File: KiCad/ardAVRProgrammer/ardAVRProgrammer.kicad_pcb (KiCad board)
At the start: 2 copper layers, 86.4 x 58.4 mm, 13 parts, among them J1 2x5_ISP_header, J2 2x3_ISP_header, U1 ATmega328-PU, U2 ATtiny2313-20PU, U3 ATtiny85-20PU

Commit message: kicad6
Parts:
- A1: footprint My_Arduino:Arduino_UNO_R3_shield_larger_pads -> My_Arduino:Arduino_UNO_R3_shield_large
- U1: value ATmega328-PU -> ATmega328P-PU
- U2: value ATtiny2313-20PU -> ATtiny2313-20M
- U3: value ATtiny85-20PU -> ATtiny85-20P; footprint My_Misc:DIP-8_W7.62mm_larger -> My_Misc:DIP-8_W7.62mm_large
- moved A1 60.0 mm to (152.4, 69.2)
- moved U1 0.10 mm to (99.7, 108.5)
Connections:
- A1 pad 1: Net-(A1-Pad1) -> unconnected-(A1-Pad1)
- A1 pad 10: Net-(A1-Pad10) -> unconnected-(A1-Pad10)
- A1 pad 11: Net-(A1-Pad11) -> unconnected-(A1-Pad11)
- A1 pad 12: Net-(A1-Pad12) -> unconnected-(A1-Pad12)
- A1 pad 13: Net-(A1-Pad13) -> unconnected-(A1-Pad13)
- A1 pad 14: Net-(A1-Pad14) -> unconnected-(A1-Pad14)
- A1 pad 15: Net-(A1-Pad15) -> unconnected-(A1-Pad15)
- A1 pad 16: Net-(A1-Pad16) -> unconnected-(A1-Pad16)
- A1 pad 17: Net-(A1-Pad17) -> unconnected-(A1-Pad17)
- A1 pad 18: Net-(A1-Pad18) -> unconnected-(A1-Pad18)
- A1 pad 19: Net-(A1-Pad19) -> unconnected-(A1-Pad19)
- A1 pad 2: Net-(A1-Pad2) -> unconnected-(A1-Pad2)
- A1 pad 20: Net-(A1-Pad20) -> unconnected-(A1-Pad20)
- A1 pad 30: Net-(A1-Pad30) -> unconnected-(A1-Pad30)
- A1 pad 31: Net-(A1-Pad31) -> unconnected-(A1-Pad31)
- A1 pad 32: Net-(A1-Pad32) -> unconnected-(A1-Pad32)
- A1 pad 4: Net-(A1-Pad4) -> unconnected-(A1-Pad4)
- A1 pad 7: Net-(A1-Pad7) -> unconnected-(A1-Pad7)
- A1 pad 8: Net-(A1-Pad8) -> unconnected-(A1-Pad8)
- A1 pad 9: Net-(A1-Pad9) -> unconnected-(A1-Pad9)
- J1 pad 3: Net-(J1-Pad3) -> unconnected-(J1-Pad3)
- U1 pad 10: Net-(U1-Pad10) -> unconnected-(U1-Pad10)
- U1 pad 11: Net-(U1-Pad11) -> unconnected-(U1-Pad11)
- U1 pad 12: Net-(U1-Pad12) -> unconnected-(U1-Pad12)
- U1 pad 13: Net-(U1-Pad13) -> unconnected-(U1-Pad13)
- U1 pad 14: Net-(U1-Pad14) -> unconnected-(U1-Pad14)
- U1 pad 15: Net-(U1-Pad15) -> unconnected-(U1-Pad15)
- U1 pad 16: Net-(U1-Pad16) -> unconnected-(U1-Pad16)
- U1 pad 2: Net-(U1-Pad2) -> unconnected-(U1-Pad2)
- U1 pad 23: Net-(U1-Pad23) -> unconnected-(U1-Pad23)
- U1 pad 24: Net-(U1-Pad24) -> unconnected-(U1-Pad24)
- U1 pad 25: Net-(U1-Pad25) -> unconnected-(U1-Pad25)
- U1 pad 26: Net-(U1-Pad26) -> unconnected-(U1-Pad26)
- U1 pad 27: Net-(U1-Pad27) -> unconnected-(U1-Pad27)
- U1 pad 28: Net-(U1-Pad28) -> unconnected-(U1-Pad28)
- U1 pad 3: Net-(U1-Pad3) -> unconnected-(U1-Pad3)
- U1 pad 4: Net-(U1-Pad4) -> unconnected-(U1-Pad4)
- U1 pad 5: Net-(U1-Pad5) -> unconnected-(U1-Pad5)
- U1 pad 6: Net-(U1-Pad6) -> unconnected-(U1-Pad6)
- U2 pad 1: Net-(A1-Pad25) -> unconnected-(U2-Pad1)
- U2 pad 10: GND -> unconnected-(U2-Pad10)
- U2 pad 11: Net-(U2-Pad11) -> unconnected-(U2-Pad11)
- U2 pad 12: Net-(U2-Pad12) -> unconnected-(U2-Pad12)
- U2 pad 13: Net-(U2-Pad13) -> unconnected-(U2-Pad13)
- U2 pad 14: Net-(U2-Pad14) -> unconnected-(U2-Pad14)
- U2 pad 15: Net-(U2-Pad15) -> Net-(A1-Pad26)
- U2 pad 16: Net-(U2-Pad16) -> Net-(A1-Pad27)
- U2 pad 17: Net-(A1-Pad26) -> Net-(A1-Pad28)
- U2 pad 18: Net-(A1-Pad27) -> +5V
- U2 pad 19: Net-(A1-Pad28) -> Net-(A1-Pad25)
- U2 pad 2: Net-(U2-Pad2) -> unconnected-(U2-Pad2)
- U2 pad 20: +5V -> unconnected-(U2-Pad20)
- U2 pad 3: Net-(U2-Pad3) -> unconnected-(U2-Pad3)
- U2 pad 4: Net-(U2-Pad4) -> unconnected-(U2-Pad4)
- U2 pad 5: Net-(U2-Pad5) -> unconnected-(U2-Pad5)
- U2 pad 6: Net-(U2-Pad6) -> unconnected-(U2-Pad6)
- U2 pad 7: Net-(U2-Pad7) -> unconnected-(U2-Pad7)
- U2 pad 8: Net-(U2-Pad8) -> GND
- U2 pad 9: Net-(U2-Pad9) -> unconnected-(U2-Pad9)
- U3 pad 2: Net-(U3-Pad2) -> unconnected-(U3-Pad2)
- U3 pad 3: Net-(U3-Pad3) -> unconnected-(U3-Pad3)
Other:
- net class Default removed

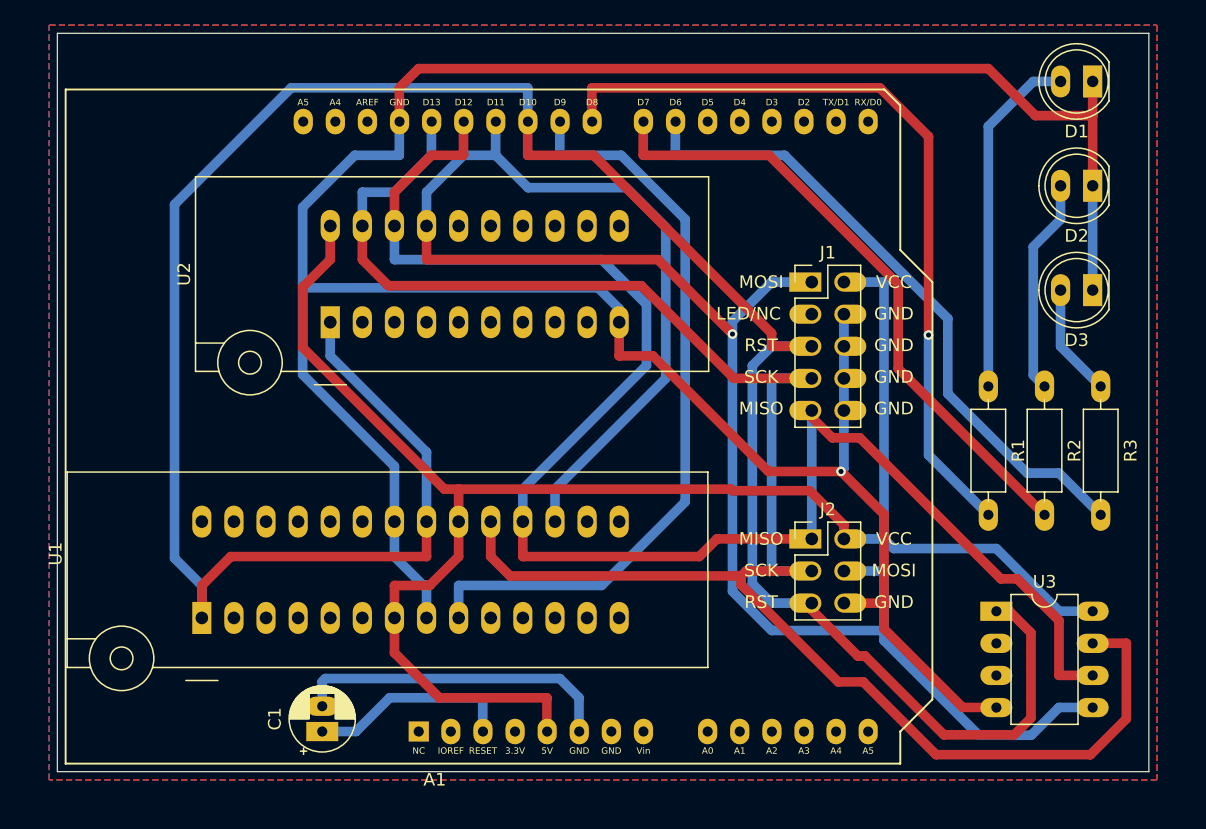
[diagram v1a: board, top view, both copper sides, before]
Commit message: new PCB layout
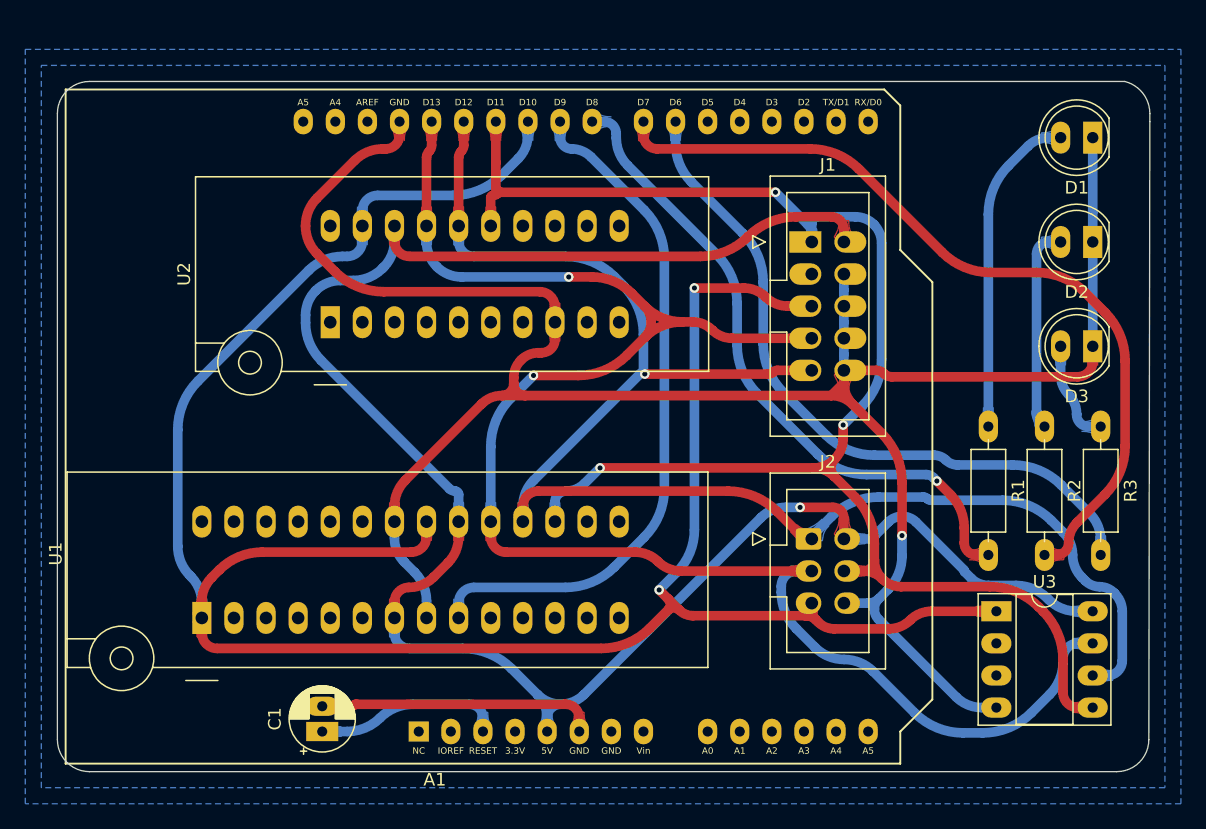
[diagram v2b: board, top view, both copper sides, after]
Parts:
- J1: footprint My_Headers:2x5_ISP_header_large -> My_Misc:IDC-Header_2x05_P2.54mm_Vertical_large
- J2: footprint My_Headers:2x3_ISP_header_large -> My_Misc:IDC-Header_2x03_P2.54mm_Vertical large
- U3: footprint My_Misc:DIP-8_W7.62mm_large -> My_Misc:DIP-8_W7.62mm_Socket_w_dip_packet_LongPads
- moved D3 4.45 mm to (170.2, 87.0)
- moved D1 4.45 mm to (170.2, 70.5)
- moved D2 4.45 mm to (170.2, 78.7)
- moved J1 3.18 mm to (148.0, 78.7)
- moved R1 3.17 mm to (161.9, 93.3)
- moved R2 3.17 mm to (166.4, 93.3)
- moved R3 3.17 mm to (170.8, 93.3)
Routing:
- net GND: track 216.9 -> 180.3 mm
- net Net-(A1-Pad26): track 155.6 -> 127.9 mm, vias 1 -> 3
- net +5V: track 138.7 -> 157.8 mm, vias 0 -> 1
- net Net-(A1-Pad25): track 203.9 -> 185.9 mm, vias 0 -> 2
- net Net-(A1-Pad28): track 151.2 -> 135.8 mm, vias 0 -> 2
- net Net-(A1-Pad22): track 50.1 -> 65.3 mm
- net Net-(A1-Pad23): track 62.8 -> 51.7 mm
- net Net-(A1-Pad24): track 60.4 -> 54.9 mm
- net Net-(A1-Pad21): track 51.6 -> 55.3 mm
- net Net-(A1-Pad27): track 127.4 -> 123.8 mm, vias 0 -> 1
- net Net-(A1-Pad6): track 25.7 -> 22.0 mm
- net Net-(D1-Pad2): track 27.8 -> 26.0 mm
- net Net-(A1-Pad3): track 16.5 -> 14.9 mm
- net Net-(D2-Pad2): track 17.1 -> 16.3 mm
- net Net-(D3-Pad2): track 8.94 -> 8.12 mm
- removed copper zone on F.Cu, net (none)
- removed copper zone on F.Cu, net GND
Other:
- board size 86.4 x 58.4 mm -> 86.4 x 54.6 mm

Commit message: new kicad
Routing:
- added copper zone on F.Cu, net (none)
- added copper zone on F.Cu, net GND
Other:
- board text added: "ardAVRProgrammer Design: Jon Sagebrand github.com/jonsag"
- board text removed: "ardAVRProgrammer Design: Jon Sagebrand jonsagebrand@gmail.com"
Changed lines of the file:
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@@
   (gr_arc (start 174.625 118.11) (mid 173.881051 119.906051) (end 172.085 120.65) (layer "Edge.Cuts") (width 0.05))
   (gr_line (start 174.703172 69.215) (end 174.703172 68.58) (layer "Edge.Cuts") (width 0.05))
-  (gr_text "ardAVRProgrammer\nDesign: Jon Sagebrand\njonsagebrand@gmail.com" (at 93.345 70.485 90) (layer "B.SilkS")
+  (gr_text "ardAVRProgrammer\nDesign: Jon Sagebrand\ngithub.com/jonsag" (at 93.345 70.485 90) (layer "B.SilkS")
     (effects (font (size 1.524 1.524) (thickness 0.2032)) (justify left mirror))
   )
@@
     )
   )
+  (zone (net 1) (net_name "GND") (layers F&B.Cu) (hatch edge 0.508)
+    (connect_pads (clearance 0.508))
+    (min_thickness 0.254) (filled_areas_thickness no)
+    (fill yes (thermal_gap 0.508) (thermal_bridge_width 0.508))
+    (polygon
+      (pts
+        (xy 175.895 121.92)
+        (xy 86.995 121.92)
+        (xy 86.995 64.77)
+        (xy 175.895 64.77)
+      )
+    )
+  )
   (zone (net 4) (net_name "Net-(A1-Pad26)") (layer "F.Cu") (hatch edge 0.508)
     (priority 16962)
@@
     )
   )
+  (zone (net 0) (net_name "") (layers F&B.Cu) (hatch edge 0.508)
+    (connect_pads (clearance 0.508))
+    (min_thickness 0.254) (filled_areas_thickness no)
+    (fill yes (thermal_gap 0.508) (thermal_bridge_width 0.508))
+    (polygon
+      (pts
+        (xy 177.165 123.19)
+        (xy 85.725 123.19)
+        (xy 85.725 63.5)
+        (xy 177.165 63.5)
+      )
+    )
+  )
   (zone (net 1) (net_name "GND") (layer "F.Cu") (hatch edge 0.508)
     (priority 16962)
@@
     )
   )
-  (zone (net 1) (net_name "GND") (layer "B.Cu") (hatch edge 0.508)
-    (connect_pads (clearance 0.508))
-    (min_thickness 0.254) (filled_areas_thickness no)
-    (fill yes (thermal_gap 0.508) (thermal_bridge_width 0.508))
-    (polygon
-      (pts
-        (xy 175.895 121.92)
-        (xy 86.995 121.92)
-        (xy 86.995 64.77)
-        (xy 175.895 64.77)
-      )
-    )
-  )
   (zone (net 11) (net_name "+5V") (layer "B.Cu") (hatch edge 0.508)
     (priority 16962)
@@
       )
     )
-  )
-  (zone (net 0) (net_name "") (layer "B.Cu") (hatch edge 0.508)
-    (connect_pads (clearance 0.508))
-    (min_thickness 0.254) (filled_areas_thickness no)
-    (fill yes (thermal_gap 0.508) (thermal_bridge_width 0.508))
-    (polygon
-      (pts
-        (xy 177.165 123.19)
-        (xy 85.725 123.19)
-        (xy 85.725 63.5)
-        (xy 177.165 63.5)
-      )
-    )

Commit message: kicad
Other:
- board text added: "${TITLE}-${REVISION} Design: Jon Sagebrand github.com/jonsag"
- board text removed: "ardAVRProgrammer Design: Jon Sagebrand github.com/jonsag"
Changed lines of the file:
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@@
   )
   (paper "A4")
+  (title_block
+    (title "ardAVRProgrammer")
+    (date "2022-09-09")
+    (rev "0.2")
+  )
   (layers
     (0 "F.Cu" signal)
@@
   (gr_arc (start 174.625 118.11) (mid 173.881051 119.906051) (end 172.085 120.65) (layer "Edge.Cuts") (width 0.05))
   (gr_line (start 174.703172 69.215) (end 174.703172 68.58) (layer "Edge.Cuts") (width 0.05))
-  (gr_text "ardAVRProgrammer\nDesign: Jon Sagebrand\ngithub.com/jonsag" (at 93.345 70.485 90) (layer "B.SilkS")
+  (gr_text "${TITLE}-${REVISION}\nDesign: Jon Sagebrand\ngithub.com/jonsag" (at 93.345 70.485 90) (layer "F.SilkS")
     (effects (font (size 1.524 1.524) (thickness 0.2032)) (justify left mirror))
   )
